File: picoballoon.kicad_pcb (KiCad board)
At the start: 2 copper layers, 85 parts, among them J1 SOLAR+, J2 SOLAR-, J3 USB_B_Micro, J4 COMMS_USART2, J5 SWD, J6 COMMS_USART3, Q1 AO3401A, Q2 DTC143ZEBTL, Q3 AO3401A, Q4 AO3401A, Q5 DTC143ZEBTL, U1 SPV1040, U2 STM32G070RBTx, U3 L70-R, U4 GPS1003, U6 Ai-Thinker-Ra-01, U7 AMS1117-3.3, U8 DHT11, Y1 Crystal

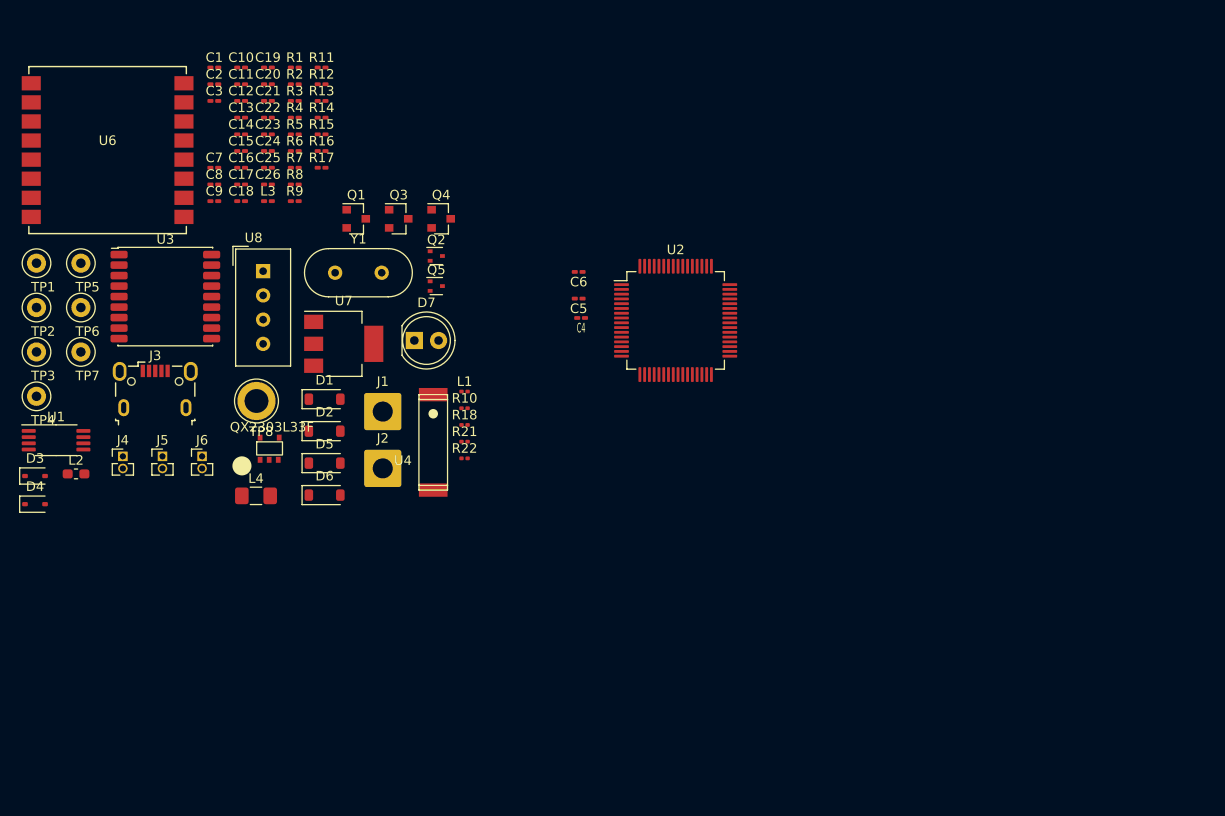
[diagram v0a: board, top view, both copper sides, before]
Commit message: Completed PCB routing
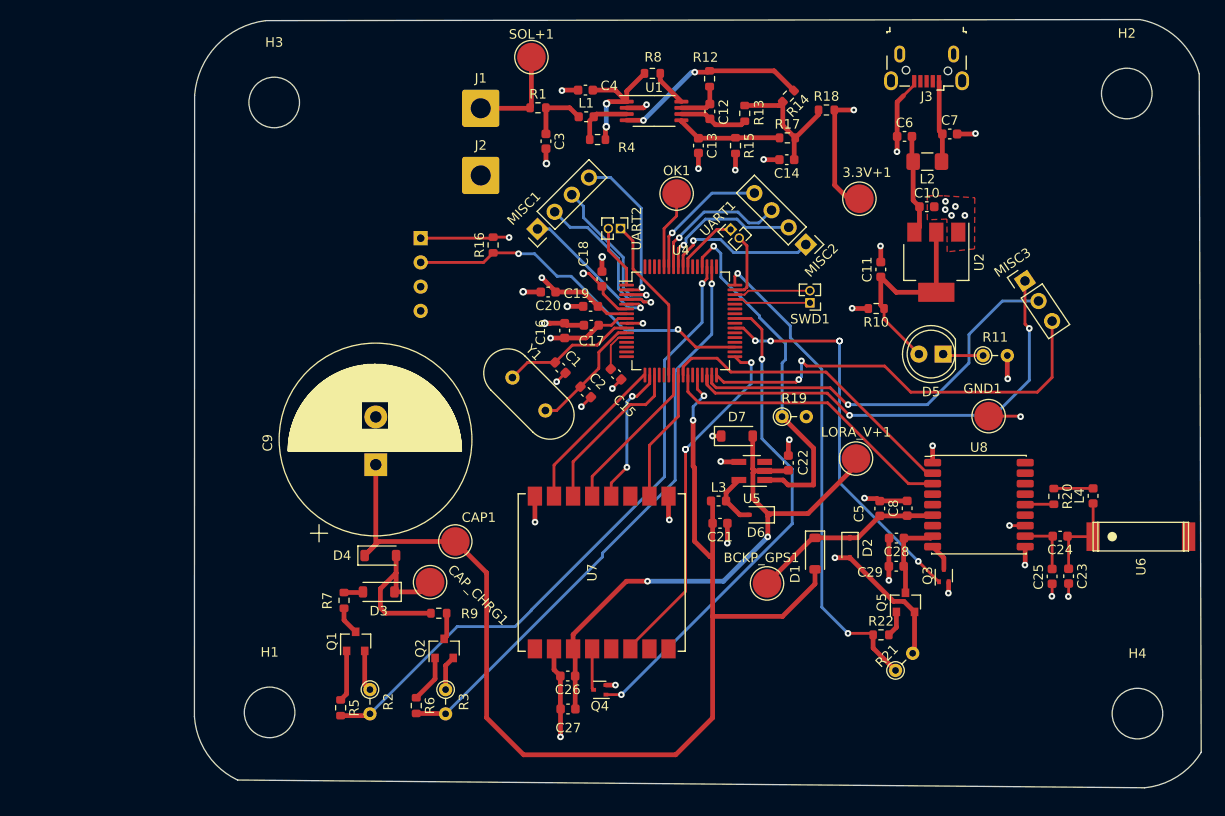
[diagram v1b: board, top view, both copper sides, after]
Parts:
- removed the R8 at (104.9, 59.4)
- added C14: 27uF, Capacitor_SMD:C_0603_1608Metric, F.Cu at (156.4, 56.8)
- added C18: 100nF, Capacitor_SMD:C_0603_1608Metric, F.Cu at (137.1, 69.3)
- added C24: 100pF, Capacitor_SMD:C_0603_1608Metric, F.Cu at (185.1, 96.3)
- added H1: MountingHole, MountingHole:MountingHole_5.3mm_M5, F.Cu at (102.2, 114.7)
- added H2: MountingHole, MountingHole:MountingHole_5.3mm_M5, F.Cu at (192.0, 49.9)
- added H3: MountingHole, MountingHole:MountingHole_5.3mm_M5, F.Cu at (102.7, 50.8)
- added H4: MountingHole, MountingHole:MountingHole_5.3mm_M5, F.Cu at (193.2, 114.9)
- added MISC1: Conn_01x04_Pin, Connector_PinHeader_2.54mm:PinHeader_1x04_P2.54mm_Vertical, F.Cu at (130.3, 64.1)
- added MISC2: Conn_01x04_Pin, Connector_PinHeader_2.54mm:PinHeader_1x04_P2.54mm_Vertical, F.Cu at (158.4, 65.7)
- added MISC3: Conn_01x03_Pin, Connector_PinHeader_2.54mm:PinHeader_1x03_P2.54mm_Vertical, F.Cu at (181.4, 69.5)
- added R1: 0, Resistor_SMD:R_0603_1608Metric, F.Cu at (130.4, 51.4)
- added R10: 0, Resistor_SMD:R_0603_1608Metric, F.Cu at (165.8, 72.4)
- added R18: 0, Resistor_SMD:R_0603_1608Metric, F.Cu at (160.6, 51.6)
- 3.3V+1: renamed from TP1; footprint TestPoint:TestPoint_Loop_D2.50mm_Drill1.0mm -> TestPoint:TestPoint_Pad_D3.0mm
- BCKP_GPS1: renamed from TP4; footprint TestPoint:TestPoint_Loop_D2.50mm_Drill1.0mm -> TestPoint:TestPoint_Pad_D3.0mm
- C1: renamed from C25; footprint Capacitor_SMD:C_0201_0603Metric_Pad0.64x0.40mm_HandSolder -> Capacitor_SMD:C_0603_1608Metric
- C10: renamed from C23; footprint Capacitor_SMD:C_0201_0603Metric_Pad0.64x0.40mm_HandSolder -> Capacitor_SMD:C_0603_1608Metric
- C11: renamed from C24; footprint Capacitor_SMD:C_0201_0603Metric_Pad0.64x0.40mm_HandSolder -> Capacitor_SMD:C_0603_1608Metric
- C12: renamed from C13; footprint Capacitor_SMD:C_0201_0603Metric_Pad0.64x0.40mm_HandSolder -> Capacitor_SMD:C_0603_1608Metric
- C13: renamed from C3; footprint Capacitor_SMD:C_0201_0603Metric_Pad0.64x0.40mm_HandSolder -> Capacitor_SMD:C_0603_1608Metric
- C15: renamed from C8; footprint Capacitor_SMD:C_0201_0603Metric_Pad0.64x0.40mm_HandSolder -> Capacitor_SMD:C_0603_1608Metric
- C16: renamed from C4; footprint Capacitor_SMD:C_0201_0603Metric_Pad0.64x0.40mm_HandSolder -> Capacitor_SMD:C_0603_1608Metric
- C17: renamed from C5; footprint Capacitor_SMD:C_0201_0603Metric_Pad0.64x0.40mm_HandSolder -> Capacitor_SMD:C_0603_1608Metric
- C19: renamed from C6; footprint Capacitor_SMD:C_0201_0603Metric_Pad0.64x0.40mm_HandSolder -> Capacitor_SMD:C_0603_1608Metric
- C2: renamed from C26; footprint Capacitor_SMD:C_0201_0603Metric_Pad0.64x0.40mm_HandSolder -> Capacitor_SMD:C_0603_1608Metric
- C20: renamed from C7; footprint Capacitor_SMD:C_0201_0603Metric_Pad0.64x0.40mm_HandSolder -> Capacitor_SMD:C_0603_1608Metric
- C21: renamed from C15; footprint Capacitor_SMD:C_0201_0603Metric_Pad0.64x0.40mm_HandSolder -> Capacitor_SMD:C_0603_1608Metric
- C22: renamed from C16; footprint Capacitor_SMD:C_0201_0603Metric_Pad0.64x0.40mm_HandSolder -> Capacitor_SMD:C_0603_1608Metric
- C23: renamed from C11; footprint Capacitor_SMD:C_0201_0603Metric_Pad0.64x0.40mm_HandSolder -> Capacitor_SMD:C_0603_1608Metric
- C25: renamed from C12; footprint Capacitor_SMD:C_0201_0603Metric_Pad0.64x0.40mm_HandSolder -> Capacitor_SMD:C_0603_1608Metric
- C26: renamed from C18; footprint Capacitor_SMD:C_0201_0603Metric_Pad0.64x0.40mm_HandSolder -> Capacitor_SMD:C_0603_1608Metric
- C27: renamed from C17; footprint Capacitor_SMD:C_0201_0603Metric_Pad0.64x0.40mm_HandSolder -> Capacitor_SMD:C_0603_1608Metric
- C28: renamed from C9; footprint Capacitor_SMD:C_0201_0603Metric_Pad0.64x0.40mm_HandSolder -> Capacitor_SMD:C_0603_1608Metric
- C29: renamed from C10; footprint Capacitor_SMD:C_0201_0603Metric_Pad0.64x0.40mm_HandSolder -> Capacitor_SMD:C_0603_1608Metric
- C3: renamed from C1; footprint Capacitor_SMD:C_0201_0603Metric_Pad0.64x0.40mm_HandSolder -> Capacitor_SMD:C_0603_1608Metric
- C4: renamed from C2; footprint Capacitor_SMD:C_0201_0603Metric_Pad0.64x0.40mm_HandSolder -> Capacitor_SMD:C_0603_1608Metric
- C5: renamed from C19; footprint Capacitor_SMD:C_0201_0603Metric_Pad0.64x0.40mm_HandSolder -> Capacitor_SMD:C_0603_1608Metric
- C6: renamed from C22; footprint Capacitor_SMD:C_0201_0603Metric_Pad0.64x0.40mm_HandSolder -> Capacitor_SMD:C_0603_1608Metric
- C7: renamed from C21; footprint Capacitor_SMD:C_0201_0603Metric_Pad0.64x0.40mm_HandSolder -> Capacitor_SMD:C_0603_1608Metric
- C8: renamed from C20; footprint Capacitor_SMD:C_0201_0603Metric_Pad0.64x0.40mm_HandSolder -> Capacitor_SMD:C_0603_1608Metric
- C9: renamed from C14; footprint Capacitor_SMD:C_0201_0603Metric_Pad0.64x0.40mm_HandSolder -> supercap:CP_Radial_D20mm_P5mm
- CAP1: renamed from TP2; footprint TestPoint:TestPoint_Loop_D2.50mm_Drill1.0mm -> TestPoint:TestPoint_Pad_D3.0mm
- CAP_CHRG1: renamed from TP6; footprint TestPoint:TestPoint_Loop_D2.50mm_Drill1.0mm -> TestPoint:TestPoint_Pad_D3.0mm
- GND1: renamed from TP7; footprint TestPoint:TestPoint_Loop_D2.50mm_Drill1.0mm -> TestPoint:TestPoint_Pad_D3.0mm
- L1: footprint Inductor_SMD:L_0201_0603Metric -> Inductor_SMD:L_0603_1608Metric
- L3: footprint Inductor_SMD:L_0201_0603Metric_Pad0.64x0.40mm_HandSolder -> Inductor_SMD:L_0603_1608Metric
- L4: renamed from L2; footprint Inductor_SMD:L_0603_1608Metric_Pad1.05x0.95mm_HandSolder -> Inductor_SMD:L_0603_1608Metric
- LORA_V+1: renamed from TP3; footprint TestPoint:TestPoint_Loop_D2.50mm_Drill1.0mm -> TestPoint:TestPoint_Pad_D3.0mm
- OK1: renamed from TP8; footprint TestPoint:TestPoint_Loop_D3.80mm_Drill2.5mm -> TestPoint:TestPoint_Pad_D3.0mm
- R11: renamed from R21; footprint Resistor_SMD:R_0201_0603Metric -> Resistor_THT:R_Axial_DIN0204_L3.6mm_D1.6mm_P2.54mm_Vertical
- R12: renamed from R10; footprint Resistor_SMD:R_0201_0603Metric -> Resistor_SMD:R_0603_1608Metric
- R13: renamed from R11; footprint Resistor_SMD:R_0201_0603Metric_Pad0.64x0.40mm_HandSolder -> Resistor_SMD:R_0603_1608Metric
- R14: renamed from R3; footprint Resistor_SMD:R_0201_0603Metric_Pad0.64x0.40mm_HandSolder -> Resistor_SMD:R_0603_1608Metric
- R15: renamed from R5; footprint Resistor_SMD:R_0201_0603Metric_Pad0.64x0.40mm_HandSolder -> Resistor_SMD:R_0603_1608Metric
- R16: renamed from R22; footprint Resistor_SMD:R_0201_0603Metric -> Resistor_SMD:R_0603_1608Metric
- R17: renamed from R4; footprint Resistor_SMD:R_0201_0603Metric_Pad0.64x0.40mm_HandSolder -> Resistor_SMD:R_0603_1608Metric
- R19: renamed from R18; footprint Resistor_SMD:R_0201_0603Metric -> Resistor_THT:R_Axial_DIN0204_L3.6mm_D1.6mm_P2.54mm_Vertical
- R2: renamed from R13; footprint Resistor_SMD:R_0201_0603Metric_Pad0.64x0.40mm_HandSolder -> Resistor_THT:R_Axial_DIN0204_L3.6mm_D1.6mm_P2.54mm_Vertical
- R20: renamed from R9; footprint Resistor_SMD:R_0201_0603Metric_Pad0.64x0.40mm_HandSolder -> Resistor_SMD:R_0603_1608Metric
- R21: renamed from R7; footprint Resistor_SMD:R_0201_0603Metric_Pad0.64x0.40mm_HandSolder -> Resistor_THT:R_Axial_DIN0204_L3.6mm_D1.6mm_P2.54mm_Vertical
- R22: renamed from R6; footprint Resistor_SMD:R_0201_0603Metric_Pad0.64x0.40mm_HandSolder -> Resistor_SMD:R_0603_1608Metric
- R3: renamed from R15; footprint Resistor_SMD:R_0201_0603Metric_Pad0.64x0.40mm_HandSolder -> Resistor_THT:R_Axial_DIN0204_L3.6mm_D1.6mm_P2.54mm_Vertical
- R4: renamed from R1; footprint Resistor_SMD:R_0201_0603Metric_Pad0.64x0.40mm_HandSolder -> Resistor_SMD:R_0603_1608Metric
- R5: renamed from R12; footprint Resistor_SMD:R_0201_0603Metric_Pad0.64x0.40mm_HandSolder -> Resistor_SMD:R_0603_1608Metric
- R6: renamed from R16; footprint Resistor_SMD:R_0201_0603Metric_Pad0.64x0.40mm_HandSolder -> Resistor_SMD:R_0603_1608Metric
- R7: renamed from R14; footprint Resistor_SMD:R_0201_0603Metric_Pad0.64x0.40mm_HandSolder -> Resistor_SMD:R_0603_1608Metric
- R8: renamed from R2; footprint Resistor_SMD:R_0201_0603Metric_Pad0.64x0.40mm_HandSolder -> Resistor_SMD:R_0603_1608Metric
- R9: renamed from R17; footprint Resistor_SMD:R_0201_0603Metric_Pad0.64x0.40mm_HandSolder -> Resistor_SMD:R_0603_1608Metric
- SOL+1: renamed from TP5; footprint TestPoint:TestPoint_Loop_D2.50mm_Drill1.0mm -> TestPoint:TestPoint_Pad_D3.0mm
- SWD1: renamed from J5; value SWD -> SWD1
- U3: renamed from U8; moved to B.Cu
- U5: footprint QX2303L33F:QX2303L33F -> Package_TO_SOT_SMD:SOT-23-5_HandSoldering
- moved L4 106.6 mm to (188.5, 92.0), turned to 90 degrees
- moved C23 100.9 mm to (186.0, 100.5), turned to -90 degrees
- moved C25 98.5 mm to (184.2, 100.5), turned to -90 degrees
- moved GND1 95.3 mm to (177.6, 83.7)
- moved U8 88.0 mm to (176.6, 93.0)
- moved J3 87.7 mm to (171.1, 46.7), turned to 180 degrees
- moved LORA_V+1 86.6 mm to (163.7, 88.1), turned to 180 degrees
- moved 3.3V+1 86.5 mm to (164.0, 60.9)
- moved C29 86.3 mm to (167.9, 99.4), turned to 180 degrees
- moved D2 85.5 mm to (163.0, 97.5), turned to -90 degrees
- moved R20 85.3 mm to (184.4, 92.1), turned to -90 degrees
- moved R21 82.1 mm to (167.8, 110.3), turned to 45 degrees
- moved C8 80.4 mm to (169.0, 93.3), turned to 90 degrees
- moved C28 79.7 mm to (167.9, 96.5), turned to 180 degrees
- moved R22 79.6 mm to (166.3, 106.6)
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- renumbered D5 to D1, D4 to D2, D2 to D3, D1 to D4, D7 to D5, D3 to D6, D6 to D7, L4 to L2, Q3 to Q1, Q4 to Q2, Q2 to Q3, Q5 to Q4, Q1 to Q5, U7 to U2, U2 to U4, U4 to U6, U6 to U7, U3 to U8, J4 to UART1, J6 to UART2
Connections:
- C11 pad 1: MCU_BACKUP -> Net-(D5-A)
- C23 pad 1: unconnected-(C11-Pad1) -> Net-(C23-Pad1)
- C3 pad 1: SOLAR+ -> Net-(C3-Pad1)
- D5 pad 2: MCU_BACKUP -> Net-(D5-A)
- L1 pad 1: SOLAR+ -> Net-(C3-Pad1)
- L4 pad 1: Net-(L2-Pad1) -> Net-(C23-Pad1)
- R13 pad 2: MCU_BACKUP -> Net-(C14-Pad1)
- R14 pad 2: MCU_BACKUP -> Net-(C14-Pad1)
- R17 pad 2: MCU_BACKUP -> Net-(C14-Pad1)
- U2 pad 2: MCU_BACKUP -> Net-(D5-A)
- U4 pad 17: unconnected-(U2-PA0-Pad17) -> LORA_SPI1_NSS
- U4 pad 2: unconnected-(U2-PC12-Pad2) -> PC12
- U4 pad 24: unconnected-(U2-PA7-Pad24) -> BUSY
- U4 pad 3: unconnected-(U2-PC13-Pad3) -> PC13
- U4 pad 30: unconnected-(U2-PB10-Pad30) -> PB10
- U4 pad 31: unconnected-(U2-PB11-Pad31) -> PB11
- U4 pad 32: LORA_SPI1_NSS -> PB12
- U4 pad 35: unconnected-(U2-PB15-Pad35) -> DHD11_DAT
- U4 pad 4: unconnected-(U2-PC14-Pad4) -> PC14
- U4 pad 41: unconnected-(U2-PD9-Pad41) -> LORA_RESET
- U4 pad 5: unconnected-(U2-PC15-Pad5) -> PC15
- U4 pad 56: LORA_RESET -> PD6
- U4 pad 57: unconnected-(U2-PB3-Pad57) -> PB3
- U4 pad 58: unconnected-(U2-PB4-Pad58) -> PB4
- U4 pad 59: unconnected-(U2-PB5-Pad59) -> PB5
- U6 pad RF_IN: unconnected-(U4-PadRF_IN) -> Net-(C23-Pad1)
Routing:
- net BCKP_OUT: track 0.00 -> 124.1 mm, vias 0 -> 2
- net GND: track 0.00 -> 84.5 mm, vias 0 -> 39
- net MCU_BACKUP: track 0.00 -> 73.9 mm, vias 0 -> 8
- net LowPowCapChrg: track 0.00 -> 68.2 mm, vias 0 -> 1
- net HighPowCapChrg: track 0.00 -> 61.5 mm, vias 0 -> 1
- net LORA_Vout: track 0.00 -> 58.7 mm, vias 0 -> 2
- net LORA_RESET: track 0.00 -> 51.9 mm, vias 0 -> 2
- net GPS_EN: track 0.00 -> 51.3 mm, vias 0 -> 2
- net PB10: track 0.00 -> 49.1 mm, vias 0 -> 2
- net PB12: track 0.00 -> 45.3 mm, vias 0 -> 2
- net PB11: track 0.00 -> 42.4 mm, vias 0 -> 1
- net GPS_RESET_SIGNAL: track 0.00 -> 41.1 mm, vias 0 -> 5
- net DC_EN: track 0.00 -> 37.6 mm, vias 0 -> 1
- net DHD11_DAT: track 0.00 -> 37.5 mm, vias 0 -> 2
- net DIO1: track 0.00 -> 37.2 mm, vias 0 -> 3
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- added copper zone on F.Cu, net GND
- added copper zone on In1.Cu, net GND
- added copper zone on In2.Cu, net MCU_BACKUP
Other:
- board outline added: 105.5 x 80.5 mm
- copper layers 2 -> 4

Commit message: PCB completed and is in production
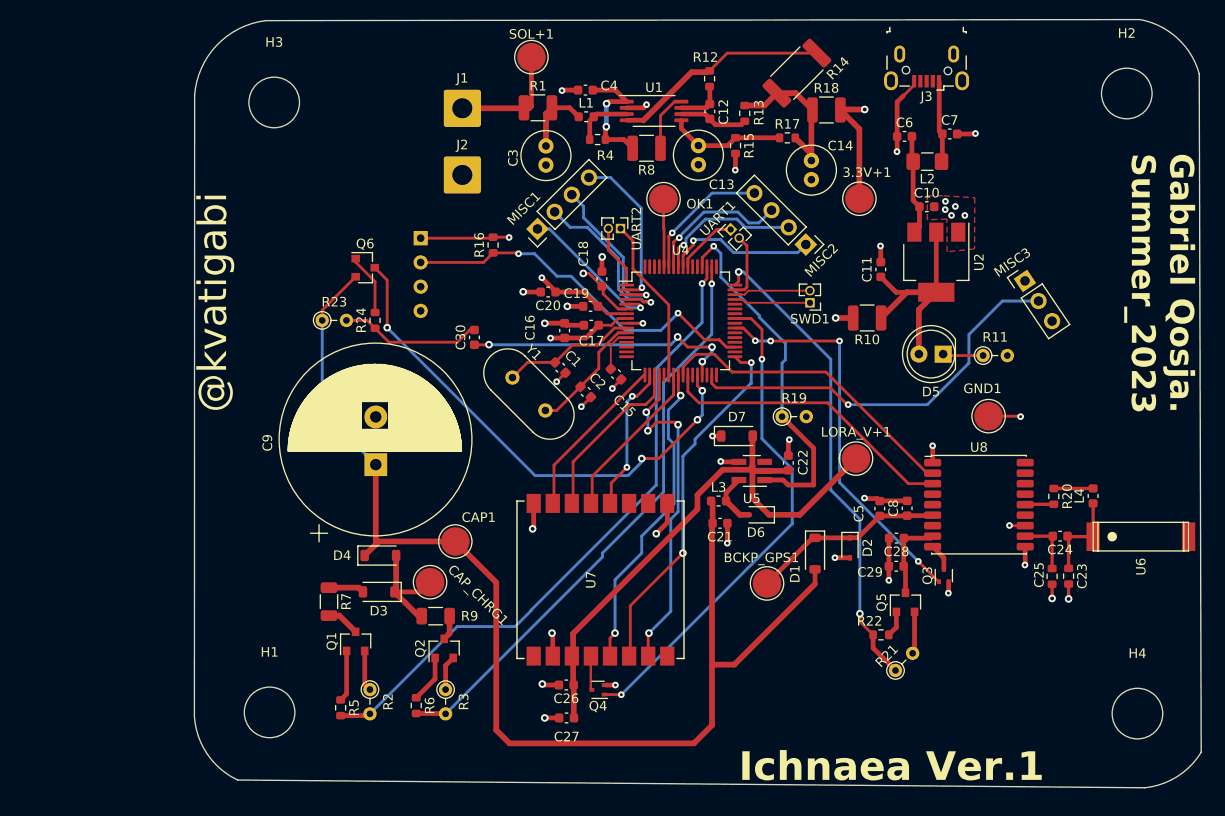
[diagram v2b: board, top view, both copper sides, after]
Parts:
- added C30: 100nF, Capacitor_SMD:C_0603_1608Metric, F.Cu at (123.7, 75.4)
- added Q6: AO3401A, Package_TO_SOT_SMD:SOT-23, F.Cu at (112.3, 68.1)
- added R23: 10K, Resistor_THT:R_Axial_DIN0204_L3.6mm_D1.6mm_P2.54mm_Vertical, F.Cu at (107.7, 73.7)
- added R24: 3.3K, Resistor_SMD:R_0603_1608Metric, F.Cu at (113.3, 73.7)
- C13: value 60uF -> 68uF; footprint Capacitor_SMD:C_0603_1608Metric -> Capacitor_THT:C_Radial_D5.0mm_H11.0mm_P2.00mm
- C14, C3: footprint Capacitor_SMD:C_0603_1608Metric -> Capacitor_THT:C_Radial_D5.0mm_H11.0mm_P2.00mm
- C2: value 2.2uF -> 16pF
- C23, C25: footprint Capacitor_SMD:C_0603_1608Metric -> Resistor_SMD:R_0603_1608Metric
- L3: value 2,05uH -> 2,2uH
- R1, R10, R18, R8: footprint Resistor_SMD:R_0603_1608Metric -> Resistor_SMD:R_1210_3225Metric
- R14: footprint Resistor_SMD:R_0603_1608Metric -> Resistor_SMD:R_2512_6332Metric
- R7, R9: footprint Resistor_SMD:R_0603_1608Metric -> Resistor_SMD:R_1206_3216Metric
- U7: value Ai-Thinker-Ra-01 -> RA-01H
- moved R8 7.87 mm to (141.7, 55.6)
- moved C14 2.58 mm to (159.0, 56.9), turned to -90 degrees
- moved R14 2.57 mm to (157.5, 47.8)
- moved J2 1.93 mm to (122.4, 58.4)
- moved J1 1.93 mm to (122.4, 51.4)
- moved R7 1.58 mm to (108.5, 103.1)
- moved OK1 1.49 mm to (143.5, 61.0)
- moved R10 1.37 mm to (164.8, 73.4)
- moved C27 0.95 mm to (133.3, 115.3)
- moved C26 0.95 mm to (133.3, 111.9)
- moved U7 0.77 mm to (136.9, 100.8)
- moved C3 0.50 mm to (131.2, 55.4)
- moved R9 0.45 mm to (119.6, 104.6)
- moved Q4 0.18 mm to (136.7, 112.4)
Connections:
- 3.3V+1 pad 1: MCU_BACKUP -> +3.3V
- C16 pad 1: MCU_BACKUP -> +3.3V
- C17 pad 1: MCU_BACKUP -> +3.3V
- C18 pad 1: MCU_BACKUP -> +3.3V
- C19 pad 1: MCU_BACKUP -> +3.3V
- C20 pad 1: MCU_BACKUP -> +3.3V
- D2 pad 2: MCU_BACKUP -> +3.3V
- D7 pad 1: MCU_BACKUP -> +3.3V
- MISC3 pad 1: PB10 -> GND
- MISC3 pad 3: PB12 -> +3.3V
- Q1 pad 2: MCU_BACKUP -> +3.3V
- Q2 pad 2: MCU_BACKUP -> +3.3V
- Q5 pad 2: MCU_BACKUP -> +3.3V
- R10 pad 2: MCU_BACKUP -> +3.3V
- R16 pad 2: MCU_BACKUP -> +3.3V
- R18 pad 2: MCU_BACKUP -> +3.3V
- R2 pad 1: MCU_BACKUP -> +3.3V
- R21 pad 2: MCU_BACKUP -> +3.3V
- R3 pad 1: MCU_BACKUP -> +3.3V
- U3 pad 1: MCU_BACKUP -> +3.3V
- U4 pad 20: unconnected-(U4-PA3-Pad20) -> DIO2
- U4 pad 24: BUSY -> DIO0
- U4 pad 28: BCKP_OUT -> CAP_CHRG_V
- U4 pad 29: unconnected-(U4-PB2-Pad29) -> CAP_CHRG_READ_EN
- U4 pad 30: PB10 -> unconnected-(U4-PB10-Pad30)
- U4 pad 6: MCU_BACKUP -> +3.3V
- U4 pad 7: MCU_BACKUP -> +3.3V
- U4 pad 8: MCU_BACKUP -> +3.3V
- U7 pad 10: BUSY -> unconnected-(U7-DIO4-Pad10)
- U7 pad 5: unconnected-(U7-TXEN-Pad5) -> DIO0
- U7 pad 7: unconnected-(U7-DIO2-Pad7) -> DIO2
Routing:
- net MCU_BACKUP: track 73.9 -> 0.00 mm, vias 8 -> 0
- net +3.3V: track 0.00 -> 64.5 mm, vias 0 -> 8
- net CAP_CHRG_V: track 0.00 -> 53.5 mm, vias 0 -> 4
- net PB10: track 49.1 -> 0.00 mm, vias 2 -> 0
- net PB12: track 45.3 -> 0.00 mm, vias 2 -> 0
- net DIO2: track 0.00 -> 35.7 mm, vias 0 -> 4
- net DIO0: track 0.00 -> 33.1 mm, vias 0 -> 2
- net CAP_CHRG_READ_EN: track 0.00 -> 29.1 mm, vias 0 -> 4
- net Net-(C30-Pad2): track 0.00 -> 14.9 mm
- net BUSY: track 13.9 -> 0.00 mm
- net GND: track 84.5 -> 73.9 mm, vias 39 -> 37
- net Net-(Q6-Pad1): track 0.00 -> 6.49 mm
- net SUPERCAP_CHRG: track 17.9 -> 11.9 mm
- net BCKP_OUT: track 124.1 -> 128.5 mm, vias 2 -> 0
- net Net-(D5-A): track 22.5 -> 26.9 mm
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- added copper zone on In2.Cu, net +3.3V
- removed copper zone on In2.Cu, net MCU_BACKUP
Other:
- board text added: "@kvatigabi"
- board text added: "Gabriel Qosja. Summer_2023"
- board text added: "Ichnaea Ver.1"
- board text added: "Φτιαγμένο στη γή από ανθρώπους."
